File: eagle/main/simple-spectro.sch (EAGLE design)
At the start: 54 parts, among them IC1 MCP1703-33, IC2 MCP1703-50, J2 RJ12RIGHTANGLE-I2C, Q1 DMP1045U, U1 MCP73831T, X2 8MHz, X4 MINI-USB

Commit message: v1.1.0 nearly final design
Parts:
- removed C4: 100nF, dp_devices:CAPACITOR_NPOL-0805
- removed RK1: 3.9k, rcl:R-EU_R0805
- removed U$12: CONN2, lpatiny:CONN2
- added A, BAT, V: (no value), jumper:JP1E
- added JP4: PS>5.5V, jumper:JP1E
- added R6: 10k, dp_devices:TRIMMER-3362P
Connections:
- new net N$17: A.2, D5.C, Q1.S
- net D10*: now also U$11.DB6; no longer U$11.DB7
- net D11*: now also R6.3; no longer 220.1
- net D12*: now also U$7.OUT; no longer U$11.E
- net D13*: now also 220.1; no longer RK1.1
- net D5*: now also U$11.DB7; no longer U$7.OUT
- net D6*: now also U$11.E; no longer U$11.DB4
- net D8*: now also U$11.DB4; no longer U$11.DB5
- net D9*: now also U$11.DB5; no longer U$11.DB6
- net GND: now also BAT.2, JP4.1, R6.1, V.2; no longer C4.2, U$12.1
- net I2C+12V: now also JP4.2
- net N$2: now also R6.2; no longer C4.1, RK1.2
- net VBAT1: now also BAT.1; no longer U$12.2
- net VCC: now also V.1
- net VDD: now also A.1; no longer D5.C, Q1.S

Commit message: v1.1.0 submitted for PCB
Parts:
- removed JP4: PS>5.5V, jumper:JP1E
- JP1: value (none) -> BAT
- JP2: value (none) -> A
- renumbered A to JP2, BAT to JP1, V to JP3
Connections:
- net GND: no longer JP4.1
- net I2C+12V: no longer JP4.2
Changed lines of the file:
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@@
 <part name="GND11" library="supply1" deviceset="GND" device=""/>
 <part name="R6" library="dp_devices" deviceset="TRIMMER" device="-3362P" value="10k"/>
-<part name="BAT" library="jumper" deviceset="JP1E" device=""/>
-<part name="A" library="jumper" deviceset="JP1E" device=""/>
-<part name="V" library="jumper" deviceset="JP1E" device=""/>
+<part name="JP1" library="jumper" deviceset="JP1E" device="" value="BAT"/>
+<part name="JP2" library="jumper" deviceset="JP1E" device="" value="A"/>
+<part name="JP3" library="jumper" deviceset="JP1E" device=""/>
 <part name="GND12" library="supply1" deviceset="GND" device=""/>
-<part name="JP4" library="jumper" deviceset="JP1E" device="" value="PS&gt;5.5V"/>
-<part name="U$6" library="microbuilder" deviceset="GND" device=""/>
 </parts>
 <sheets>
@@
 <instance part="GND11" gate="1" x="182.88" y="248.92"/>
 <instance part="R6" gate="R" x="137.16" y="50.8" rot="R90"/>
-<instance part="BAT" gate="A" x="325.12" y="170.18" rot="R270"/>
-<instance part="A" gate="A" x="340.36" y="167.64" rot="R90"/>
-<instance part="V" gate="A" x="43.18" y="53.34" rot="R270"/>
+<instance part="JP1" gate="A" x="325.12" y="170.18" rot="R270"/>
+<instance part="JP2" gate="A" x="340.36" y="167.64" rot="R90"/>
+<instance part="JP3" gate="A" x="43.18" y="53.34" rot="R270"/>
 <instance part="GND12" gate="1" x="43.18" y="43.18" smashed="yes">
 <attribute name="VALUE" x="41.275" y="41.275" size="1.27" layer="96"/>
 </instance>
-<instance part="JP4" gate="A" x="205.74" y="193.04" rot="R270"/>
-<instance part="U$6" gate="G$1" x="198.12" y="187.96"/>
 </instances>
 <busses>
@@
 <wire x1="350.52" y1="162.56" x2="350.52" y2="157.48" width="0.1524" layer="91"/>
 <junction x="322.58" y="157.48"/>
-<pinref part="BAT" gate="A" pin="2"/>
+<pinref part="JP1" gate="A" pin="2"/>
 </segment>
 <segment>
@@
 </segment>
 <segment>
-<pinref part="V" gate="A" pin="2"/>
+<pinref part="JP3" gate="A" pin="2"/>
 <wire x1="40.64" y1="50.8" x2="40.64" y2="45.72" width="0.1524" layer="91"/>
 <pinref part="GND12" gate="1" pin="GND"/>
 <wire x1="40.64" y1="45.72" x2="43.18" y2="45.72" width="0.1524" layer="91"/>
-</segment>
-<segment>
-<pinref part="JP4" gate="A" pin="1"/>
-<wire x1="203.2" y1="193.04" x2="198.12" y2="193.04" width="0.1524" layer="91"/>
-<wire x1="198.12" y1="193.04" x2="198.12" y2="190.5" width="0.1524" layer="91"/>
-<pinref part="U$6" gate="G$1" pin="GND"/>
 </segment>
 </net>
@@
 <pinref part="Q1" gate="G$1" pin="D"/>
 <wire x1="314.96" y1="175.26" x2="327.66" y2="175.26" width="0.1524" layer="91"/>
-<pinref part="BAT" gate="A" pin="1"/>
+<pinref part="JP1" gate="A" pin="1"/>
 </segment>
 </net>
@@
 </segment>
 <segment>
-<pinref part="A" gate="A" pin="1"/>
+<pinref part="JP2" gate="A" pin="1"/>
 <pinref part="SUPPLY4" gate="G$1" pin="VDD"/>
 <wire x1="342.9" y1="167.64" x2="342.9" y2="162.56" width="0.1524" layer="91"/>
@@
 <wire x1="30.48" y1="43.18" x2="38.1" y2="43.18" width="0.1524" layer="91"/>
 <wire x1="38.1" y1="43.18" x2="38.1" y2="53.34" width="0.1524" layer="91"/>
-<pinref part="V" gate="A" pin="1"/>
+<pinref part="JP3" gate="A" pin="1"/>
 <wire x1="38.1" y1="53.34" x2="40.64" y2="53.34" width="0.1524" layer="91"/>
 <junction x="38.1" y="43.18"/>
@@
 <segment>
 <pinref part="IC2" gate="G$1" pin="VI"/>
-<wire x1="200.66" y1="182.88" x2="203.2" y2="182.88" width="0.1524" layer="91"/>
+<wire x1="200.66" y1="182.88" x2="215.9" y2="182.88" width="0.1524" layer="91"/>
 <label x="200.66" y="180.34" size="1.778" layer="95"/>
-<pinref part="JP4" gate="A" pin="2"/>
-<wire x1="203.2" y1="182.88" x2="215.9" y2="182.88" width="0.1524" layer="91"/>
-<wire x1="203.2" y1="190.5" x2="203.2" y2="182.88" width="0.1524" layer="91"/>
-<junction x="203.2" y="182.88"/>
 </segment>
 </net>
@@
 <pinref part="D5" gate="G$1" pin="C"/>
 <wire x1="342.9" y1="175.26" x2="342.9" y2="177.8" width="0.1524" layer="91"/>
-<pinref part="A" gate="A" pin="2"/>
+<pinref part="JP2" gate="A" pin="2"/>
 <wire x1="342.9" y1="170.18" x2="342.9" y2="175.26" width="0.1524" layer="91"/>
 </segment>

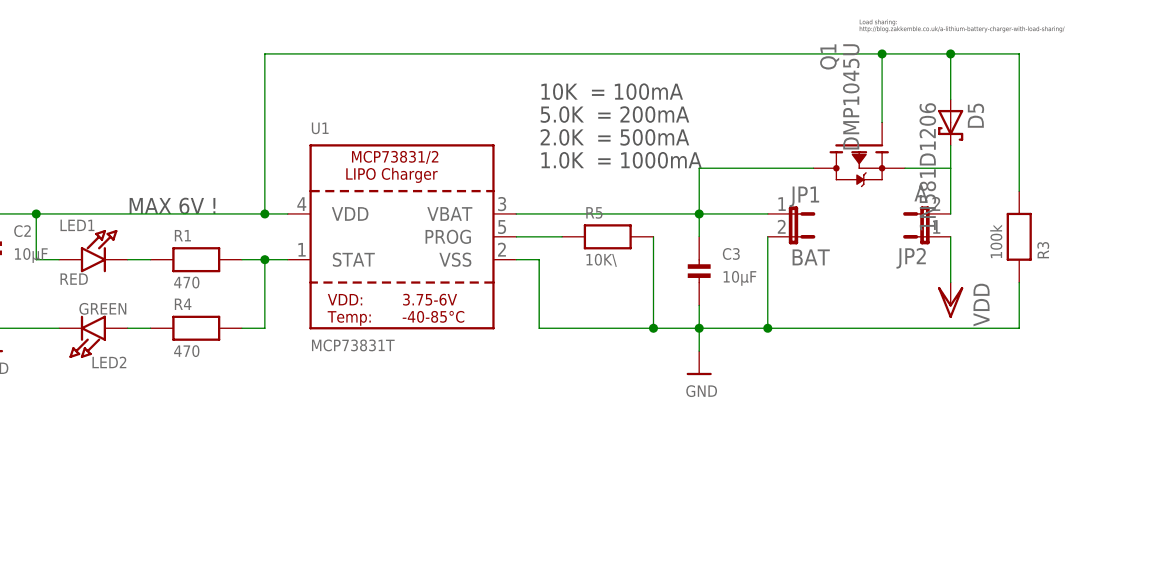
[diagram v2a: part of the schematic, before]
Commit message: work to move components to 1206
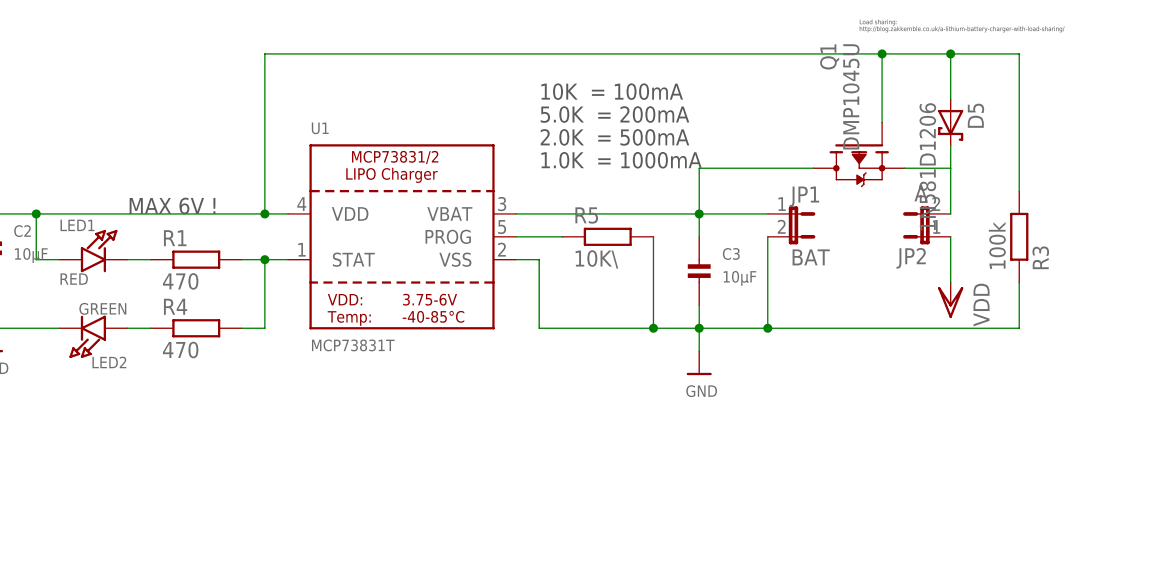
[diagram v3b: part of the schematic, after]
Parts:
- 220, R2, R9, RL2, RL3, RL4, RXT: device rcl:R-EU_R0805 -> rcl:R-EU_M1206
- C10, C12, C13, CX1, CX2: device rcl:C-EUC1206 -> resistor:C-EUC1206
- CU1, CU7, CU8: device rcl:C-EUC0805 -> resistor:C-EUC1206
- R1, R3, R4, R5: device microbuilder:RESISTOR0805 -> rcl:R-EU_M1206
- R13: device resistor:R-EU_R0805 -> rcl:R-EU_M1206
- RK3, RK7: device resistor:R-EU_M0805 -> rcl:R-EU_M1206
- RUSB1, RUSB2: device resistor:R-EU_M1206 -> rcl:R-EU_M1206
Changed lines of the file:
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@@
 <?xml version="1.0" encoding="utf-8"?>
 <!DOCTYPE eagle SYSTEM "eagle.dtd">
-<eagle version="7.7.0">
+<eagle version="8.3.1">
 <drawing>
 <settings>
 <setting alwaysvectorfont="yes"/>
+<setting keepoldvectorfont="yes"/>
 <setting verticaltext="up"/>
 </settings>
@@
 <part name="CON_ISP" library="lpatiny" deviceset="TINYISP" device="T" value="SPI"/>
 <part name="GND14" library="supply1" deviceset="GND" device=""/>
-<part name="R13" library="resistor" deviceset="R-EU_" device="R0805" value="1k"/>
+<part name="R13" library="rcl" deviceset="R-EU_" device="M1206" package3d_urn="urn:adsk.eagle:package:23566/1" value="1k"/>
 <part name="X4" library="con-cypressindustries" deviceset="MINI-USB-SCHIELD-" device="32005-201" value="MINI-USB"/>
-<part name="RUSB2" library="resistor" deviceset="R-EU_" device="M1206" value="22"/>
-<part name="RUSB1" library="resistor" deviceset="R-EU_" device="M1206" value="22"/>
-<part name="C10" library="rcl" deviceset="C-EU" device="C1206" value="100nF"/>
+<part name="RUSB2" library="rcl" deviceset="R-EU_" device="M1206" package3d_urn="urn:adsk.eagle:package:23566/1" value="22"/>
+<part name="RUSB1" library="rcl" deviceset="R-EU_" device="M1206" package3d_urn="urn:adsk.eagle:package:23566/1" value="22"/>
+<part name="C10" library="resistor" library_urn="urn:adsk.eagle:library:348" deviceset="C-EU" device="C1206" package3d_urn="urn:adsk.eagle:package:26140/1" value="100nF"/>
 <part name="32U4" library="adafruit" deviceset="ATMEGA32U4" device="-AU" value="32U4"/>
-<part name="CX2" library="rcl" deviceset="C-EU" device="C1206" value="22pF"/>
-<part name="CX1" library="rcl" deviceset="C-EU" device="C1206" value="22pF"/>
+<part name="CX2" library="resistor" library_urn="urn:adsk.eagle:library:348" deviceset="C-EU" device="C1206" package3d_urn="urn:adsk.eagle:package:26140/1" value="22pF"/>
+<part name="CX1" library="resistor" library_urn="urn:adsk.eagle:library:348" deviceset="C-EU" device="C1206" package3d_urn="urn:adsk.eagle:package:26140/1" value="22pF"/>
 <part name="U$10" library="MyPOW" deviceset="VUSB" device=""/>
-<part name="RK7" library="resistor" deviceset="R-EU_" device="M0805" value="10k"/>
-<part name="C13" library="rcl" deviceset="C-EU" device="C1206" value="100nF"/>
+<part name="RK7" library="rcl" deviceset="R-EU_" device="M1206" value="10k"/>
+<part name="C13" library="resistor" library_urn="urn:adsk.eagle:library:348" deviceset="C-EU" device="C1206" package3d_urn="urn:adsk.eagle:package:26140/1" value="100nF"/>
 <part name="X2" library="lpatiny" deviceset="XTAL" device="NX6035" value="8MHz"/>
 <part name="SUPPLY6" library="supply1" deviceset="VCC" device=""/>
 <part name="SUPPLY7" library="supply1" deviceset="VCC" device=""/>
-<part name="C12" library="rcl" deviceset="C-EU" device="C1206" value="100nF"/>
+<part name="C12" library="resistor" library_urn="urn:adsk.eagle:library:348" deviceset="C-EU" device="C1206" package3d_urn="urn:adsk.eagle:package:26140/1" value="100nF"/>
 <part name="LDPW5" library="adafruit" deviceset="LED" device="CHIP-LED0805" value="RED"/>
 <part name="GND5" library="supply1" deviceset="GND" device=""/>
@@
 <part name="GND45" library="supply1" deviceset="GND" device=""/>
 <part name="GND54" library="supply1" deviceset="GND" device=""/>
-<part name="RXT" library="rcl" deviceset="R-EU_" device="R0805" value="1M"/>
+<part name="RXT" library="rcl" library_urn="urn:adsk.eagle:library:334" deviceset="R-EU_" device="M1206" package3d_urn="urn:adsk.eagle:package:23566/1" value="1M"/>
 <part name="SUPPLY18" library="supply1" deviceset="VCC" device=""/>
 <part name="GND1" library="supply1" deviceset="GND" device=""/>
@@
 <part name="GND3" library="supply1" deviceset="GND" device=""/>
 <part name="GND4" library="supply1" deviceset="GND" device=""/>
-<part name="220" library="rcl" deviceset="R-EU_" device="R0805" value="220"/>
+<part name="220" library="rcl" deviceset="R-EU_" device="M1206" value="220"/>
 <part name="U$1" library="lpatiny" deviceset="EC11E" device=""/>
 <part name="GND7" library="supply1" deviceset="GND" device=""/>
@@
 <part name="LED1" library="microbuilder" deviceset="LED" device="0805" value="RED"/>
 <part name="LED2" library="microbuilder" deviceset="LED" device="0805" value="GREEN"/>
-<part name="R1" library="microbuilder" deviceset="RESISTOR" device="0805" value="470"/>
-<part name="R4" library="microbuilder" deviceset="RESISTOR" device="0805" value="470"/>
+<part name="R1" library="rcl" deviceset="R-EU_" device="M1206" package3d_urn="urn:adsk.eagle:package:23566/1" value="470"/>
+<part name="R4" library="rcl" deviceset="R-EU_" device="M1206" package3d_urn="urn:adsk.eagle:package:23566/1" value="470"/>
 <part name="C2" library="microbuilder" deviceset="CAP_CERAMIC" device="0805" value="10µF"/>
 <part name="U$3" library="microbuilder" deviceset="GND" device=""/>
 <part name="C3" library="microbuilder" deviceset="CAP_CERAMIC" device="0805" value="10µF"/>
 <part name="U$5" library="microbuilder" deviceset="GND" device=""/>
-<part name="R5" library="microbuilder" deviceset="RESISTOR" device="0805" value="10K\"/>
-<part name="RL2" library="rcl" deviceset="R-EU_" device="R0805" value="150"/>
-<part name="RL3" library="rcl" deviceset="R-EU_" device="R0805" value="100"/>
-<part name="RL4" library="rcl" deviceset="R-EU_" device="R0805" value="150"/>
+<part name="R5" library="rcl" deviceset="R-EU_" device="M1206" package3d_urn="urn:adsk.eagle:package:23566/1" value="10K\"/>
+<part name="RL2" library="rcl" deviceset="R-EU_" device="M1206" value="150"/>
+<part name="RL3" library="rcl" deviceset="R-EU_" device="M1206" value="100"/>
+<part name="RL4" library="rcl" deviceset="R-EU_" device="M1206" value="150"/>
 <part name="U$9" library="lpatiny" deviceset="RGB-COMMON-CATHODE" device=""/>
 <part name="R7" library="rcl" deviceset="R-EU_" device="R0805" value="1k"/>
@@
 <part name="BKLD1" library="adafruit" deviceset="LED" device="CHIP-LED0805" value="RED"/>
 <part name="U$11" library="HD44780LCD" deviceset="LCD-HD44780" device="16X2-4-HOLES" technology="4-HOLES"/>
-<part name="CU7" library="rcl" deviceset="C-EU" device="C0805" value="10u"/>
+<part name="CU7" library="resistor" library_urn="urn:adsk.eagle:library:348" deviceset="C-EU" device="C1206" package3d_urn="urn:adsk.eagle:package:26140/1" value="10u"/>
 <part name="GND19" library="supply1" deviceset="GND" device=""/>
-<part name="CU8" library="rcl" deviceset="C-EU" device="C0805" value="10u"/>
+<part name="CU8" library="resistor" library_urn="urn:adsk.eagle:library:348" deviceset="C-EU" device="C1206" package3d_urn="urn:adsk.eagle:package:26140/1" value="10u"/>
 <part name="IC1" library="linear" deviceset="MCP1703" device="DB" value="MCP1703-33"/>
 <part name="SUPPLY3" library="supply1" deviceset="VDD" device=""/>
@@
 <part name="P+1" library="supply1" deviceset="VCC" device=""/>
 <part name="Q1" library="dp_devices" deviceset="TRANSISTOR_FET_TSM2301CX" device="" value="DMP1045U"/>
-<part name="R3" library="microbuilder" deviceset="RESISTOR" device="0805" value="100k"/>
+<part name="R3" library="rcl" deviceset="R-EU_" device="M1206" package3d_urn="urn:adsk.eagle:package:23566/1" value="100k"/>
 <part name="D5" library="lpatiny" deviceset="1N581*" device="D1206" value="1N581D1206"/>
 <part name="SUPPLY4" library="supply1" deviceset="VDD" device=""/>
 <part name="U$2" library="MyPOW" deviceset="VUSB" device=""/>
 <part name="D4" library="lpatiny" deviceset="1N581*" device="D1206" value="1N581D1206"/>
-<part name="R9" library="rcl" deviceset="R-EU_" device="R0805" value="1k"/>
+<part name="R9" library="rcl" deviceset="R-EU_" device="M1206" value="1k"/>
 <part name="GND9" library="supply1" deviceset="GND" device=""/>
 <part name="L1" library="SparkFun" deviceset="LED" device="5MM" value="UV"/>
@@
 <part name="D7" library="lpatiny" deviceset="1N581*" device="D1206" value="1N581D1206"/>
 <part name="D8" library="lpatiny" deviceset="1N581*" device="D1206" value="1N581D1206"/>
-<part name="CU1" library="rcl" deviceset="C-EU" device="C0805" value="100nF"/>
-<part name="RK3" library="resistor" deviceset="R-EU_" device="M0805" value="100k"/>
+<part name="CU1" library="resistor" library_urn="urn:adsk.eagle:library:348" deviceset="C-EU" device="C1206" package3d_urn="urn:adsk.eagle:package:26140/1" value="100nF"/>
+<part name="RK3" library="rcl" library_urn="urn:adsk.eagle:library:334" deviceset="R-EU_" device="M1206" package3d_urn="urn:adsk.eagle:package:23566/1" value="100k"/>
 <part name="IC2" library="linear" deviceset="MCP1703" device="DB" value="MCP1703-50"/>
 <part name="U$4" library="microbuilder" deviceset="GND" device=""/>
-<part name="R2" library="rcl" deviceset="R-EU_" device="R0805" value="1k"/>
+<part name="R2" library="rcl" deviceset="R-EU_" device="M1206" value="1k"/>
 <part name="GND10" library="supply1" deviceset="GND" device=""/>
 <part name="L2" library="led" deviceset="LED" device="3MM" value="UV"/>
@@
 which will not be processed correctly with this version.
 </note>
+<note version="8.2" severity="warning">
+Since Version 8.2, EAGLE supports online libraries. The ids
+of those online libraries will not be understood (or retained)
+with this version.
+</note>
+<note version="8.3" severity="warning">
+Since Version 8.3, EAGLE supports URNs for individual library
+assets (packages, symbols, and devices). The URNs of those assets
+will not be understood (or retained) with this version.
+</note>
+<note version="8.3" severity="warning">
+Since Version 8.3, EAGLE supports the association of 3D packages
+with devices in libraries, schematics, and board files. Those 3D
+packages will not be understood (or retained) with this version.
+</note>
 </compatibility>

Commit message: final version of eagle v1.2.0
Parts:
- removed BKLD1: RED, adafruit:LEDCHIP-LED0805
- removed D7: 1N581D1206, lpatiny:1N581D1206
- removed IC2: MCP1703-50, linear:MCP1703DB
- removed J2: RJ12RIGHTANGLE-I2C, lpatiny:RJ12RIGHTANGLE-I2C
- removed R7: 1k, rcl:R-EU_R0805
- C2, C3: device microbuilder:CAP_CERAMIC0805 -> dp_devices:CAPACITOR_NPOL-1206
- LDPW5: device adafruit:LEDCHIP-LED0805 -> SparkFun:LED1206
- LED1, LED2: device microbuilder:LED0805 -> SparkFun:LED1206
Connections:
- removed net I2C+12V: IC2.VI, J2.1
- removed net I2C+5V: D7.A, J2.5
- removed net N$14: BKLD1.A, R7.2
- net A5: no longer R7.1
- net GND: now also C2.2, C3.2; no longer BKLD1.C, C2.P$2, C3.P$2, IC2.GND, J2.4, J2.6
- net N$15: now also C2.1; no longer C2.P$1, D7.C, IC2.VO
- net SCL: no longer J2.2
- net SDA: no longer J2.3
- net VBAT1: now also C3.1; no longer C3.P$1
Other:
- note removed: "I2C Slave"

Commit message: improve look of schema
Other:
- note added: "Light to freq."
- note added: "Power supply"
- moved on the sheet: 32U4, C10, C12, C13, C2, C3, CON_ISP, CON_ISP1, CX1, CX2, D4, D5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
